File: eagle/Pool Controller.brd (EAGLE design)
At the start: 67.3 x 64.4 mm, 27 parts, among them J1 POWER_JACKPTH, J2 Temp_Pool, J3 Relay, J4 Solar_Mon, J5 Temp_Solar

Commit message: Finished initial design
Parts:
- added POOL_CONTROLLER: PHOTON_WITH_HEADERS, Spark:PHOTON
- added U$7: (no value), holes:2,8
- U$1: value PHOTON_WITH_HEADERS -> (none); device Spark:PHOTON -> holes:2,8
- moved J2 56.2 mm to (27.9, 69.8), turned to 180 degrees
- moved J4 53.5 mm to (53.3, 69.8), turned to 180 degrees
- moved J5 51.2 mm to (40.6, 69.8), turned to 180 degrees
- moved U$1 50.2 mm to (17.1, 10.8), turned to 0 degrees
- moved R4 48.7 mm to (11.4, 54.6), turned to 0 degrees
- moved R5 47.4 mm to (12.7, 47.0), turned to 90 degrees
- moved J3 10.2 mm to (62.2, 39.4)
- moved U$4 1.27 mm to (3.81, 5.08)
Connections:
- removed net VCC: R4.1
- net 3.3V: now also POOL_CONTROLLER.24, R4.1; no longer U$1.24
- net GND: now also POOL_CONTROLLER.2, POOL_CONTROLLER.21; no longer U$1.2, U$1.21
- net N$1: now also POOL_CONTROLLER.15; no longer U$1.15
- net N$11: now also POOL_CONTROLLER.10; no longer U$1.10
- net N$12: now also POOL_CONTROLLER.9; no longer U$1.9
- net N$14: now also POOL_CONTROLLER.12; no longer U$1.12
- net N$2: now also POOL_CONTROLLER.16; no longer U$1.16
- net N$3: now also POOL_CONTROLLER.13; no longer U$1.13
- net N$4: now also POOL_CONTROLLER.14; no longer U$1.14
- net N$5: now also POOL_CONTROLLER.11; no longer U$1.11
- net N$6: now also POOL_CONTROLLER.17; no longer U$1.17
- net N$7: now also POOL_CONTROLLER.18; no longer U$1.18
- net N$9: now also POOL_CONTROLLER.19; no longer U$1.19
- net VBAT: now also POOL_CONTROLLER.22; no longer U$1.22
- net VIN: now also POOL_CONTROLLER.1; no longer U$1.1
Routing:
- net N$12: track 0.00 -> 185.1 mm
- net N$11: track 0.00 -> 152.7 mm
- net 3.3V: track 106.6 -> 166.4 mm, vias 1 -> 0
- net N$9: track 34.6 -> 81.5 mm
- net N$5: track 49.8 -> 22.1 mm
- net 5V: track 83.5 -> 100.3 mm
- net N$1: track 52.7 -> 39.8 mm
- net N$2: track 47.7 -> 36.9 mm
- net N$7: track 39.4 -> 30.4 mm
- net N$6: track 42.6 -> 33.6 mm
- net N$14: track 134.3 -> 142.2 mm
- net N$15: track 35.8 -> 42.8 mm
- net N$4: track 12.7 -> 8.64 mm
- net N$13: track 60.5 -> 64.0 mm
- net N$8: track 49.5 -> 47.0 mm
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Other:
- board size 67.3 x 64.4 mm -> 67.3 x 70.8 mm

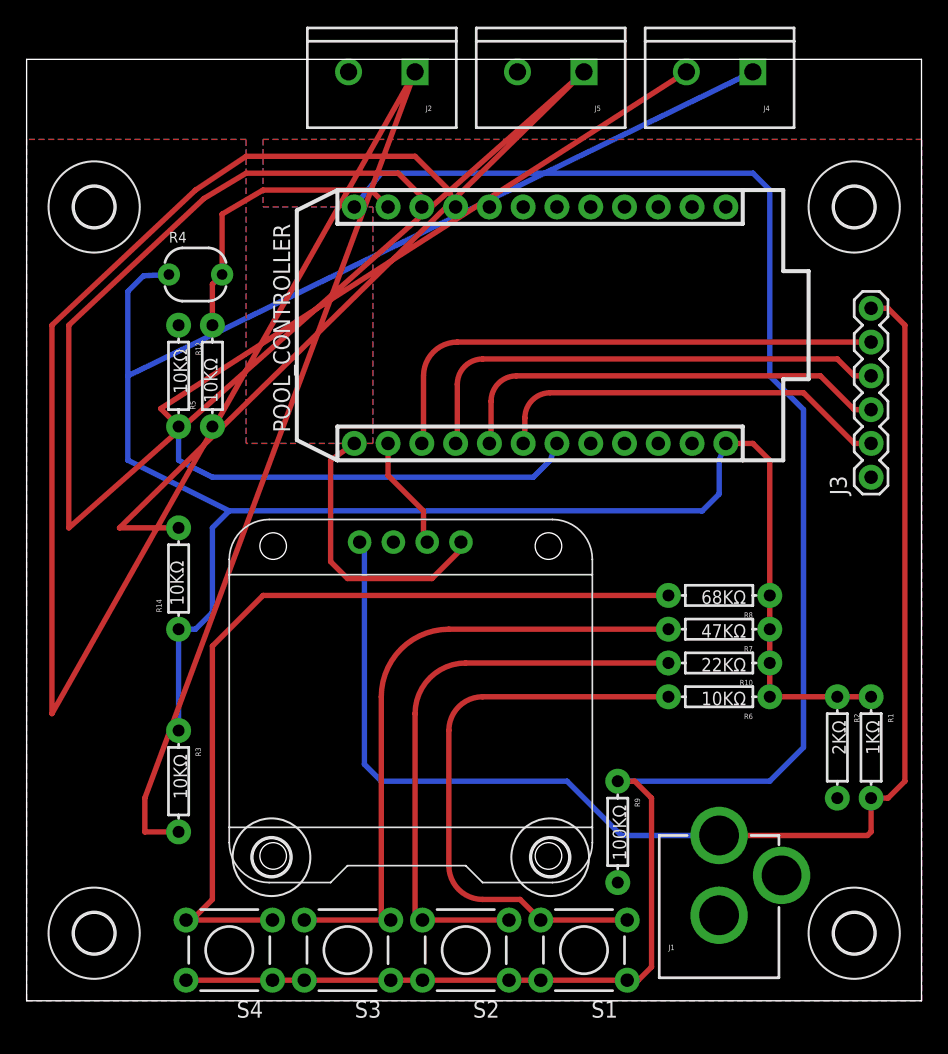
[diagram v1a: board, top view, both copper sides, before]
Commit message: Updated Eagle files for PCB v2.1
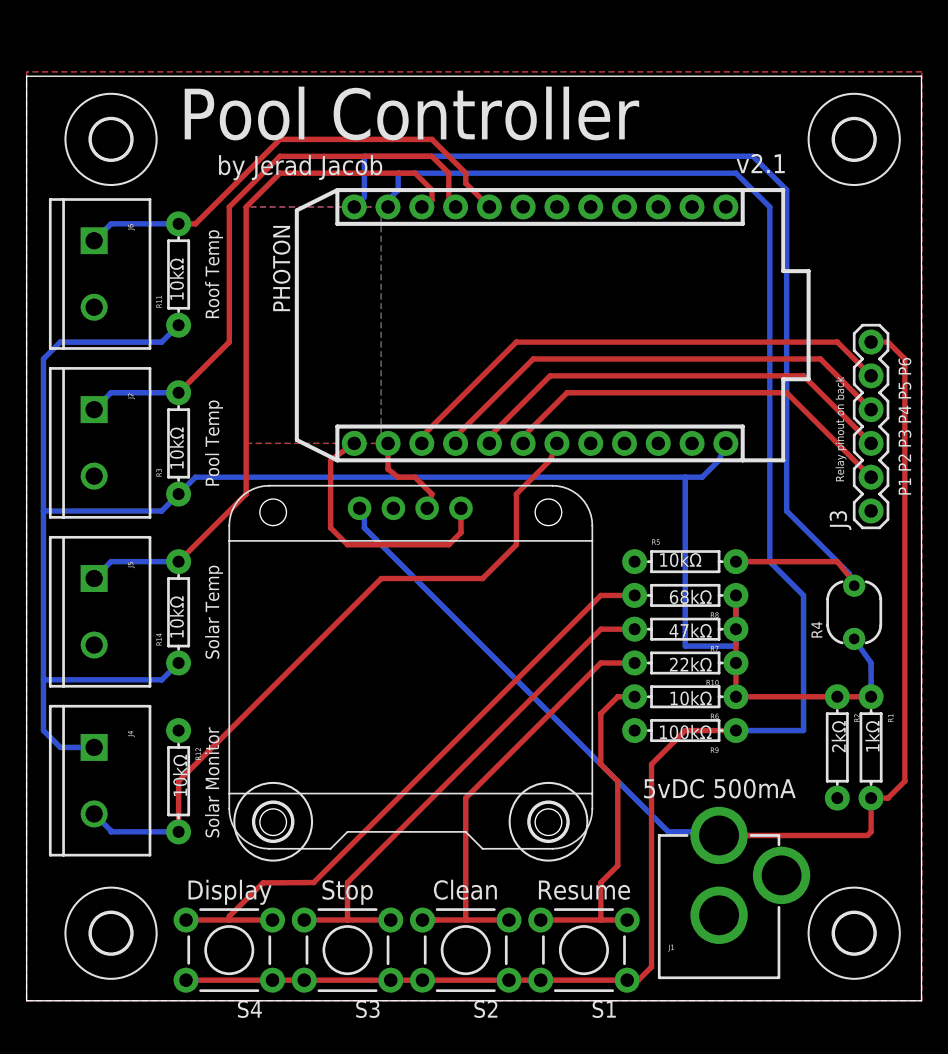
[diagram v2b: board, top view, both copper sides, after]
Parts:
- added J6: Temp_Roof, SparkFun-Connectors:SCREWTERMINAL-5MM-2
- added R11: 10kΩ, SparkFun-Passives:AXIAL-0.3
- J3: value Relay -> (none)
- PHOTON: value PHOTON_WITH_HEADERS -> (none)
- R1: value 1KΩ -> 1kΩ
- R10: value 22KΩ -> 22kΩ
- R12, R14, R3, R5, R6: value 10KΩ -> 10kΩ
- R2: value 2KΩ -> 2kΩ
- R4: value PHOTOCELLPTH -> PHOTOCELL
- R7: value 47KΩ -> 47kΩ
- R8: value 68KΩ -> 68kΩ
- R9: value 100KΩ -> 100kΩ
- moved J4 70.9 mm to (3.81, 19.1), turned to 270 degrees
- moved R4 55.7 mm to (61.0, 29.2), turned to 90 degrees
- moved J5 53.0 mm to (3.81, 31.8), turned to 270 degrees
- moved R5 38.2 mm to (48.3, 33.0), turned to 0 degrees
- moved J2 35.0 mm to (3.81, 44.5), turned to 270 degrees
- moved R12 30.5 mm to (10.2, 16.5)
- moved R3 25.4 mm to (10.2, 41.9), turned to 90 degrees
- moved R9 9.16 mm to (48.3, 20.3), turned to 180 degrees
- moved U$3 5.24 mm to (5.08, 64.8)
- moved U$6 5.08 mm to (61.0, 64.8)
- moved U$7 2.67 mm to (38.0, 13.5)
- moved U$1 2.67 mm to (17.3, 13.5)
- moved J3 2.54 mm to (62.2, 36.8)
- moved R10 2.54 mm to (48.3, 25.4)
- moved R14 2.54 mm to (10.2, 29.2)
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- renumbered POOL_CONTROLLER to PHOTON
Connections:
- new net N$17: J6.1, PHOTON.8, R11.P$2
- net 3.3V: now also R11.P$1
- net GND: now also J6.2
- net N$14: now also PHOTON.11; no longer PHOTON.12
- net N$5: now also PHOTON.12; no longer PHOTON.11
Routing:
- net N$12: track 185.1 -> 43.8 mm
- net N$11: track 152.7 -> 52.9 mm
- net N$5: track 22.1 -> 78.5 mm
- net N$17: track 0.00 -> 35.4 mm
- net N$9: track 81.5 -> 52.3 mm
- net N$15: track 42.8 -> 26.1 mm
- net N$13: track 64.0 -> 48.1 mm
- net 3.3V: track 166.4 -> 150.8 mm
- net 5V: track 100.3 -> 89.8 mm
- net N$10: track 43.0 -> 33.0 mm
- net N$8: track 47.0 -> 38.8 mm
- net N$14: track 142.2 -> 135.4 mm
- net N$3: track 21.6 -> 19.8 mm
- net N$1: track 39.8 -> 38.3 mm
- net N$4: track 8.64 -> 7.10 mm
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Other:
- board size 67.3 x 70.8 mm -> 67.3 x 69.5 mm
- board text added: "5vDC 500mA"
- board text added: "African Black-footed penguins, although they cannot fly, can swim up to 25 miles per hour which is faster than the Atlantic Bottlenosed dolphin, which can attain speeds of 18-23 mph."
- board text added: "Clean"
- board text added: "Display"
- board text added: "P1 P2 P3 P4 P5 P6"
- board text added: "Pool Controller"
- board text added: "Pool Temp"
- board text added: "RELAY PINOUT: P1 GND P2 Solar P3 Pump Relay 3 P4 Pump Relay 2 P5 Pump Relay 1 P6 VCC (5V)"
- board text added: "Relay pinout on back"
- board text added: "Resume"
- board text added: "Roof Temp"
- board text added: "Solar Monitor"
- board text added: "Solar Temp"
- board text added: "Stop"
- board text added: "by Jerad Jacob"
- board text added: "github.com/Here-Be-Dragons"
- board text added: "v2.1"

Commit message: Added 3.3v Regulator
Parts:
- removed R1: 1kΩ, SparkFun-Passives:AXIAL-0.3
- removed R2: 2kΩ, SparkFun-Passives:AXIAL-0.3
- added IC1: LM1117T-3.3, lm1117:TO220V
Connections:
- net 3.3V: now also IC1.2; no longer R1.P$1, R2.P$1
- net 5V: now also IC1.3; no longer R1.P$2
- net GND: now also IC1.1; no longer R2.P$2
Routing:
- net 3.3V: track 150.8 -> 154.5 mm
- net 5V: track 89.8 -> 90.7 mm
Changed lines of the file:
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@@
 <attribute name="STOREFRONT_ID" value="PRT-08432" x="3.81" y="31.75" size="1.778" layer="27" rot="R270" display="off"/>
 </element>
-<element name="R1" library="SparkFun-Passives" package="AXIAL-0.3" value="1kΩ" x="62.23" y="19.05" rot="R270"/>
 <element name="R10" library="SparkFun-Passives" package="AXIAL-0.3" value="22kΩ" x="48.26" y="25.4" rot="R180"/>
 <element name="R12" library="SparkFun-Passives" package="AXIAL-0.3" value="10kΩ" x="10.16" y="16.51" rot="R270"/>
 <element name="R14" library="SparkFun-Passives" package="AXIAL-0.3" value="10kΩ" x="10.16" y="29.21" rot="R90"/>
-<element name="R2" library="SparkFun-Passives" package="AXIAL-0.3" value="2kΩ" x="59.69" y="19.05" rot="R270"/>
 <element name="R3" library="SparkFun-Passives" package="AXIAL-0.3" value="10kΩ" x="10.16" y="41.91" rot="R90"/>
 <element name="R4" library="SparkFun-Sensors" package="PHOTOCELL" value="PHOTOCELL" x="60.96" y="29.21" rot="R90"/>
@@
 </element>
 <element name="R11" library="SparkFun-Passives" package="AXIAL-0.3" value="10kΩ" x="10.16" y="54.61" rot="R90"/>
+<element name="IC1" library="lm1117" package="TO220V" value="LM1117T-3.3" x="64.77" y="19.05" rot="R270"/>
 </elements>
 <signals>
@@
 <contactref element="J1" pad="GNDBREAK"/>
 <contactref element="J1" pad="GND"/>
-<contactref element="R2" pad="P$2"/>
 <contactref element="PHOTON" pad="21"/>
 <contactref element="R9" pad="P$2"/>
@@
 <vertex x="25.4" y="59.69"/>
 </polygon>
+<contactref element="IC1" pad="1"/>
 </signal>
 <signal name="N$3">
@@
 <signal name="5V">
 <contactref element="J1" pad="PWR"/>
-<contactref element="R1" pad="P$2"/>
 <contactref element="U$2" pad="VCC"/>
 <contactref element="J3" pad="6"/>
-<wire x1="50.8" y1="12.43" x2="61.96" y2="12.43" width="0.4064" layer="1"/>
-<wire x1="61.96" y1="12.43" x2="62.23" y2="12.7" width="0.4064" layer="1"/>
-<wire x1="62.23" y1="12.7" x2="62.23" y2="15.24" width="0.4064" layer="1"/>
-<wire x1="62.23" y1="15.24" x2="63.5" y2="15.24" width="0.4064" layer="1"/>
-<wire x1="63.5" y1="15.24" x2="64.77" y2="16.51" width="0.4064" layer="1"/>
+<wire x1="50.8" y1="12.43" x2="62.23" y2="12.43" width="0.4064" layer="1"/>
 <wire x1="64.77" y1="16.51" x2="64.77" y2="48.26" width="0.4064" layer="1"/>
 <wire x1="64.77" y1="48.26" x2="63.5" y2="49.53" width="0.4064" layer="1"/>
@@
 <wire x1="23.77" y1="37.03" x2="24.13" y2="36.83" width="0.4064" layer="16"/>
 <wire x1="24.13" y1="36.83" x2="24.13" y2="35.56" width="0.4064" layer="16"/>
+<contactref element="IC1" pad="3"/>
+<wire x1="64.77" y1="16.51" x2="62.23" y2="16.51" width="0.4064" layer="1"/>
+<wire x1="62.23" y1="12.43" x2="62.23" y2="16.51" width="0.4064" layer="1"/>
 </signal>
 <signal name="N$1">
@@
 <contactref element="R8" pad="P$1"/>
 <contactref element="R10" pad="P$1"/>
-<contactref element="R2" pad="P$1"/>
-<contactref element="R1" pad="P$1"/>
 <contactref element="PHOTON" pad="24"/>
 <contactref element="J4" pad="1"/>
 <contactref element="R3" pad="P$1"/>
-<wire x1="62.23" y1="22.86" x2="59.69" y2="22.86" width="0.4064" layer="1"/>
 <wire x1="52.07" y1="22.86" x2="52.07" y2="25.4" width="0.4064" layer="1"/>
 <wire x1="52.07" y1="25.4" x2="52.07" y2="27.94" width="0.4064" layer="1"/>
@@
 <wire x1="50.8" y1="40.64" x2="49.53" y2="39.37" width="0.4064" layer="16"/>
 <wire x1="49.53" y1="39.37" x2="48.26" y2="39.37" width="0.4064" layer="16"/>
-<wire x1="60.96" y1="27.21" x2="62.23" y2="25.4" width="0.4064" layer="16"/>
-<wire x1="62.23" y1="25.4" x2="62.23" y2="22.86" width="0.4064" layer="16"/>
-<wire x1="59.69" y1="22.86" x2="52.07" y2="22.86" width="0.4064" layer="1"/>
+<contactref element="IC1" pad="2"/>
+<wire x1="62.23" y1="19.05" x2="59.69" y2="19.05" width="0.4064" layer="1"/>
+<wire x1="59.69" y1="19.05" x2="55.88" y2="22.86" width="0.4064" layer="1"/>
+<wire x1="55.88" y1="22.86" x2="52.07" y2="22.86" width="0.4064" layer="1"/>
+<wire x1="60.96" y1="27.21" x2="60.23" y2="27.21" width="0.4064" layer="1"/>
+<wire x1="60.23" y1="27.21" x2="55.88" y2="22.86" width="0.4064" layer="1"/>
 </signal>
 <signal name="N$15">

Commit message: Revert "Added 3.3v Regulator"
This reverts commit 23a2b24274d4a83250f4b2e9a9d27c3bcc80a4d5.
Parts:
- removed IC1: LM1117T-3.3, lm1117:TO220V
- added R1: 1kΩ, SparkFun-Passives:AXIAL-0.3
- added R2: 2kΩ, SparkFun-Passives:AXIAL-0.3
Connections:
- net 3.3V: now also R1.P$1, R2.P$1; no longer IC1.2
- net 5V: now also R1.P$2; no longer IC1.3
- net GND: now also R2.P$2; no longer IC1.1
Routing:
- net 3.3V: track 154.5 -> 150.8 mm
- net 5V: track 90.7 -> 89.8 mm
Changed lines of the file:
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@@
 <attribute name="STOREFRONT_ID" value="PRT-08432" x="3.81" y="31.75" size="1.778" layer="27" rot="R270" display="off"/>
 </element>
+<element name="R1" library="SparkFun-Passives" package="AXIAL-0.3" value="1kΩ" x="62.23" y="19.05" rot="R270"/>
 <element name="R10" library="SparkFun-Passives" package="AXIAL-0.3" value="22kΩ" x="48.26" y="25.4" rot="R180"/>
 <element name="R12" library="SparkFun-Passives" package="AXIAL-0.3" value="10kΩ" x="10.16" y="16.51" rot="R270"/>
 <element name="R14" library="SparkFun-Passives" package="AXIAL-0.3" value="10kΩ" x="10.16" y="29.21" rot="R90"/>
+<element name="R2" library="SparkFun-Passives" package="AXIAL-0.3" value="2kΩ" x="59.69" y="19.05" rot="R270"/>
 <element name="R3" library="SparkFun-Passives" package="AXIAL-0.3" value="10kΩ" x="10.16" y="41.91" rot="R90"/>
 <element name="R4" library="SparkFun-Sensors" package="PHOTOCELL" value="PHOTOCELL" x="60.96" y="29.21" rot="R90"/>
@@
 </element>
 <element name="R11" library="SparkFun-Passives" package="AXIAL-0.3" value="10kΩ" x="10.16" y="54.61" rot="R90"/>
-<element name="IC1" library="lm1117" package="TO220V" value="LM1117T-3.3" x="64.77" y="19.05" rot="R270"/>
 </elements>
 <signals>
@@
 <contactref element="J1" pad="GNDBREAK"/>
 <contactref element="J1" pad="GND"/>
+<contactref element="R2" pad="P$2"/>
 <contactref element="PHOTON" pad="21"/>
 <contactref element="R9" pad="P$2"/>
@@
 <vertex x="25.4" y="59.69"/>
 </polygon>
-<contactref element="IC1" pad="1"/>
 </signal>
 <signal name="N$3">
@@
 <signal name="5V">
 <contactref element="J1" pad="PWR"/>
+<contactref element="R1" pad="P$2"/>
 <contactref element="U$2" pad="VCC"/>
 <contactref element="J3" pad="6"/>
-<wire x1="50.8" y1="12.43" x2="62.23" y2="12.43" width="0.4064" layer="1"/>
+<wire x1="50.8" y1="12.43" x2="61.96" y2="12.43" width="0.4064" layer="1"/>
+<wire x1="61.96" y1="12.43" x2="62.23" y2="12.7" width="0.4064" layer="1"/>
+<wire x1="62.23" y1="12.7" x2="62.23" y2="15.24" width="0.4064" layer="1"/>
+<wire x1="62.23" y1="15.24" x2="63.5" y2="15.24" width="0.4064" layer="1"/>
+<wire x1="63.5" y1="15.24" x2="64.77" y2="16.51" width="0.4064" layer="1"/>
 <wire x1="64.77" y1="16.51" x2="64.77" y2="48.26" width="0.4064" layer="1"/>
 <wire x1="64.77" y1="48.26" x2="63.5" y2="49.53" width="0.4064" layer="1"/>
@@
 <wire x1="23.77" y1="37.03" x2="24.13" y2="36.83" width="0.4064" layer="16"/>
 <wire x1="24.13" y1="36.83" x2="24.13" y2="35.56" width="0.4064" layer="16"/>
-<contactref element="IC1" pad="3"/>
-<wire x1="64.77" y1="16.51" x2="62.23" y2="16.51" width="0.4064" layer="1"/>
-<wire x1="62.23" y1="12.43" x2="62.23" y2="16.51" width="0.4064" layer="1"/>
 </signal>
 <signal name="N$1">
@@
 <contactref element="R8" pad="P$1"/>
 <contactref element="R10" pad="P$1"/>
+<contactref element="R2" pad="P$1"/>
+<contactref element="R1" pad="P$1"/>
 <contactref element="PHOTON" pad="24"/>
 <contactref element="J4" pad="1"/>
 <contactref element="R3" pad="P$1"/>
+<wire x1="62.23" y1="22.86" x2="59.69" y2="22.86" width="0.4064" layer="1"/>
 <wire x1="52.07" y1="22.86" x2="52.07" y2="25.4" width="0.4064" layer="1"/>
 <wire x1="52.07" y1="25.4" x2="52.07" y2="27.94" width="0.4064" layer="1"/>
@@
 <wire x1="50.8" y1="40.64" x2="49.53" y2="39.37" width="0.4064" layer="16"/>
 <wire x1="49.53" y1="39.37" x2="48.26" y2="39.37" width="0.4064" layer="16"/>
-<contactref element="IC1" pad="2"/>
-<wire x1="62.23" y1="19.05" x2="59.69" y2="19.05" width="0.4064" layer="1"/>
-<wire x1="59.69" y1="19.05" x2="55.88" y2="22.86" width="0.4064" layer="1"/>
-<wire x1="55.88" y1="22.86" x2="52.07" y2="22.86" width="0.4064" layer="1"/>
-<wire x1="60.96" y1="27.21" x2="60.23" y2="27.21" width="0.4064" layer="1"/>
-<wire x1="60.23" y1="27.21" x2="55.88" y2="22.86" width="0.4064" layer="1"/>
+<wire x1="60.96" y1="27.21" x2="62.23" y2="25.4" width="0.4064" layer="16"/>
+<wire x1="62.23" y1="25.4" x2="62.23" y2="22.86" width="0.4064" layer="16"/>
+<wire x1="59.69" y1="22.86" x2="52.07" y2="22.86" width="0.4064" layer="1"/>
 </signal>
 <signal name="N$15">

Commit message: corrected relay pinout
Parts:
- removed R1: 1kΩ, SparkFun-Passives:AXIAL-0.3
- removed R2: 2kΩ, SparkFun-Passives:AXIAL-0.3
- added IC1: LM1117T-3.3, lm1117:TO220V
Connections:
- net 3.3V: now also IC1.2; no longer R1.P$1, R2.P$1
- net 5V: now also IC1.3, J3.1; no longer J3.6, R1.P$2
- net GND: now also IC1.1, J3.6; no longer J3.1, R2.P$2
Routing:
- net 5V: track 89.8 -> 78.0 mm
- net 3.3V: track 150.8 -> 154.5 mm
- net N$6: track 33.2 -> 32.2 mm
- net N$1: track 38.3 -> 37.2 mm
- net N$2: track 35.7 -> 34.7 mm
- net N$7: track 30.7 -> 29.6 mm
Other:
- board text added: "RELAY PINOUT: P1 VCC (5V) P2 Pump Relay 1 P3 Pump Relay 2 P4 Pump Relay 3 P5 Solar P6 GND"
- board text added: "v2.2"
- board text removed: "RELAY PINOUT: P1 GND P2 Solar P3 Pump Relay 3 P4 Pump Relay 2 P5 Pump Relay 1 P6 VCC (5V)"
- board text removed: "v2.1"
